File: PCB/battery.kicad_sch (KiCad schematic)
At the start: 1 part

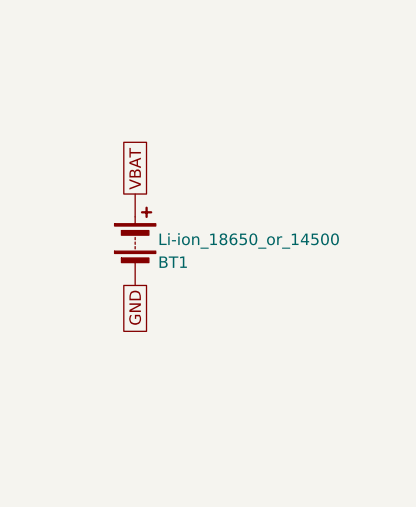
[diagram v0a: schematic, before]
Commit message: refactor: updated gulikit footprint
This updates the gulikit thumbstick footprint to be accurate.
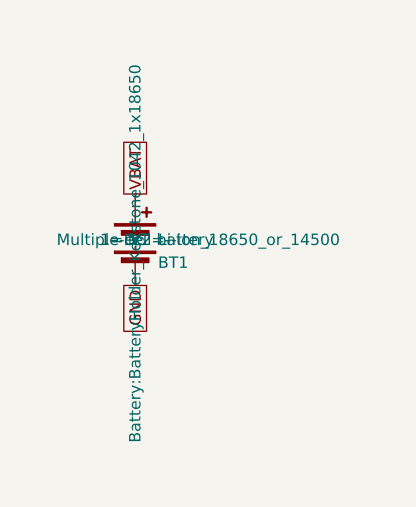
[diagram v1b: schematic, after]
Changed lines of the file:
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@@
 		(property "Footprint" "Battery:BatteryHolder_Keystone_1042_1x18650"
 			(at 148.59 106.934 90)
-			(hide yes)
 			(show_name no)
 			(do_not_autoplace no)
@@
 		(property "Datasheet" ""
 			(at 148.59 106.934 90)
-			(hide yes)
 			(show_name no)
 			(do_not_autoplace no)
@@
 		(property "Description" "Multiple-cell battery"
 			(at 148.59 105.41 0)
-			(hide yes)
 			(show_name no)
 			(do_not_autoplace no)
@@
 		(property "Sim.Device" "V"
 			(at 148.59 105.41 0)
-			(hide yes)
 			(show_name no)
 			(do_not_autoplace no)
@@
 		(property "Sim.Type" "DC"
 			(at 148.59 105.41 0)
-			(hide yes)
 			(show_name no)
 			(do_not_autoplace no)
@@
 		(property "Sim.Pins" "1=+ 2=-"
 			(at 148.59 105.41 0)
-			(hide yes)
 			(show_name no)
 			(do_not_autoplace no)
@@
 		)
 		(instances
-			(project "snips_controller"
-				(path "/868f8289-8434-4465-b2f4-2accc5e40bab/748cb1dd-d7df-4e73-a93b-27e67a5ba349"
+			(project ""
+				(path "/d0f5b7d7-b2b6-4492-958c-e60265d3c6b4/1c35c5cf-c022-4f34-b463-7ba7d15d3ffa"
 					(reference "BT1")
 					(unit 1)
